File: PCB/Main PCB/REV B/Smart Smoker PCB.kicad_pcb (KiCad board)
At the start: 4 copper layers, 100 x 100 mm, 161 parts, among them J1 393570002, J10 Spare2, J2 Conn_01x03_Female, J3 1051330001, J4 Hopper, J5 393570002, J6 393570002, J7 Screen, J8 393570002, J9 Spare1, Q1 2N7002, Q2 2N7002, Q3 MBT3904DW1, Q4 2N7002, U1 AMS1117-3.3, U10 ALDP105W, U11 TLP2362TPR_E, U12 ALDP105W, U13 STM811SW16F, U2 TS5A23159DGS, U3 ESP32-WROOM-32UE_16MB, U4 MAX31855KASA, U5 TPS2115APWR, U6 TLP2362TPR_E, U7 ALDP105W, U8 CP2102N-A02-GQFN24, U9 TLP2362TPR_E

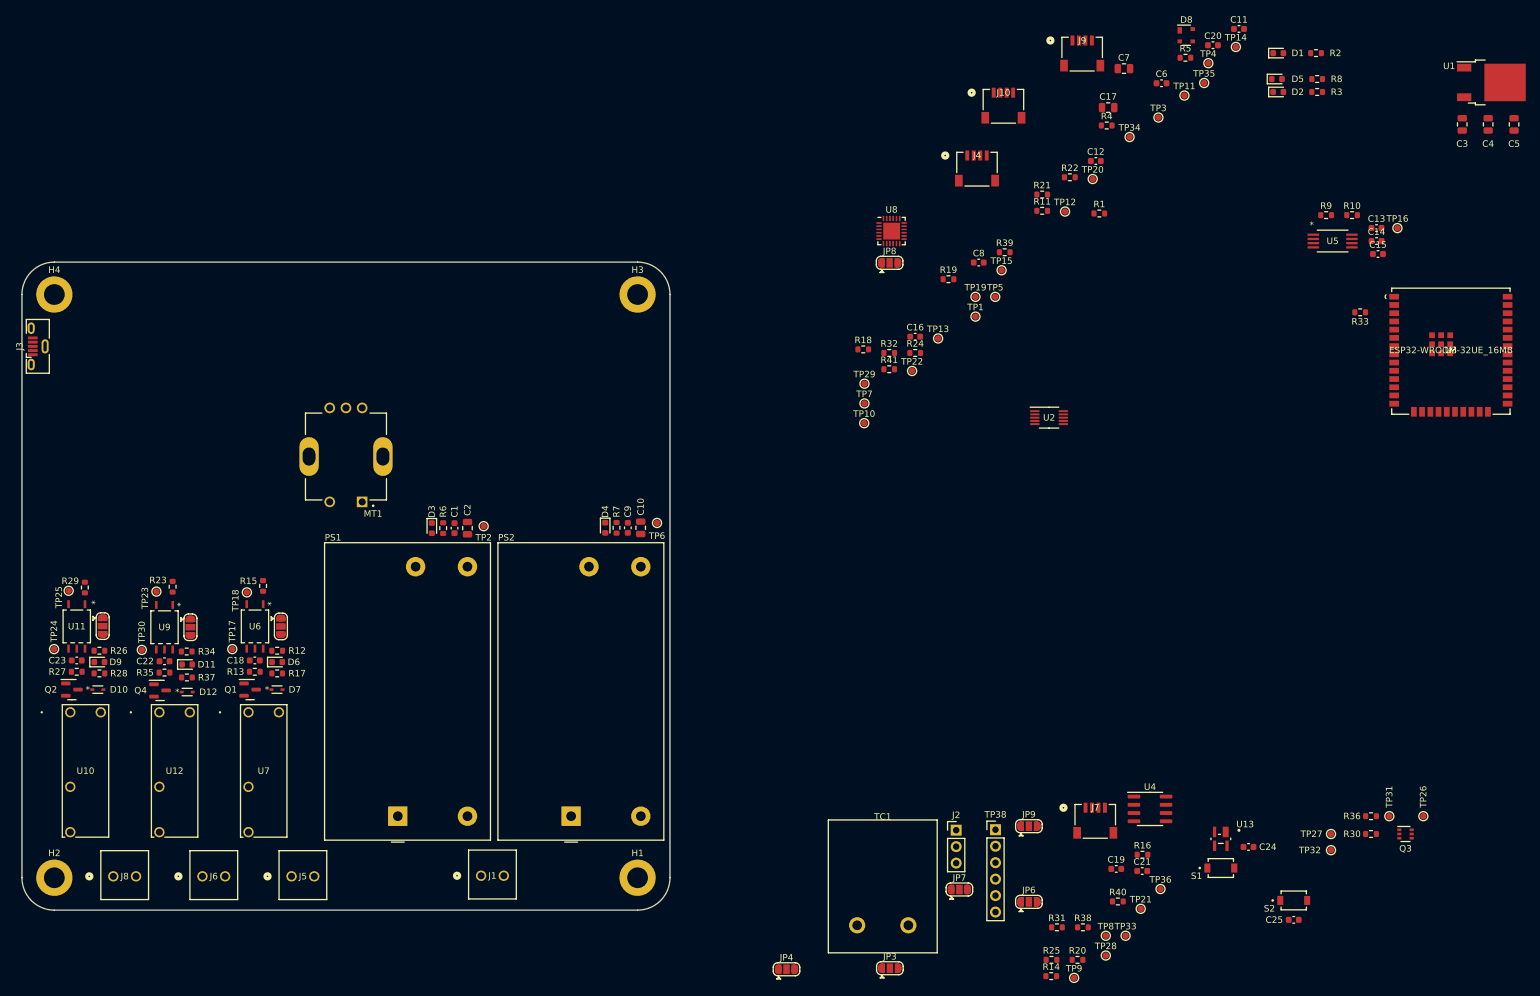
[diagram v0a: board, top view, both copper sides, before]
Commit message: PCB Layout - Work on rotary footprint, change usb to horizontal
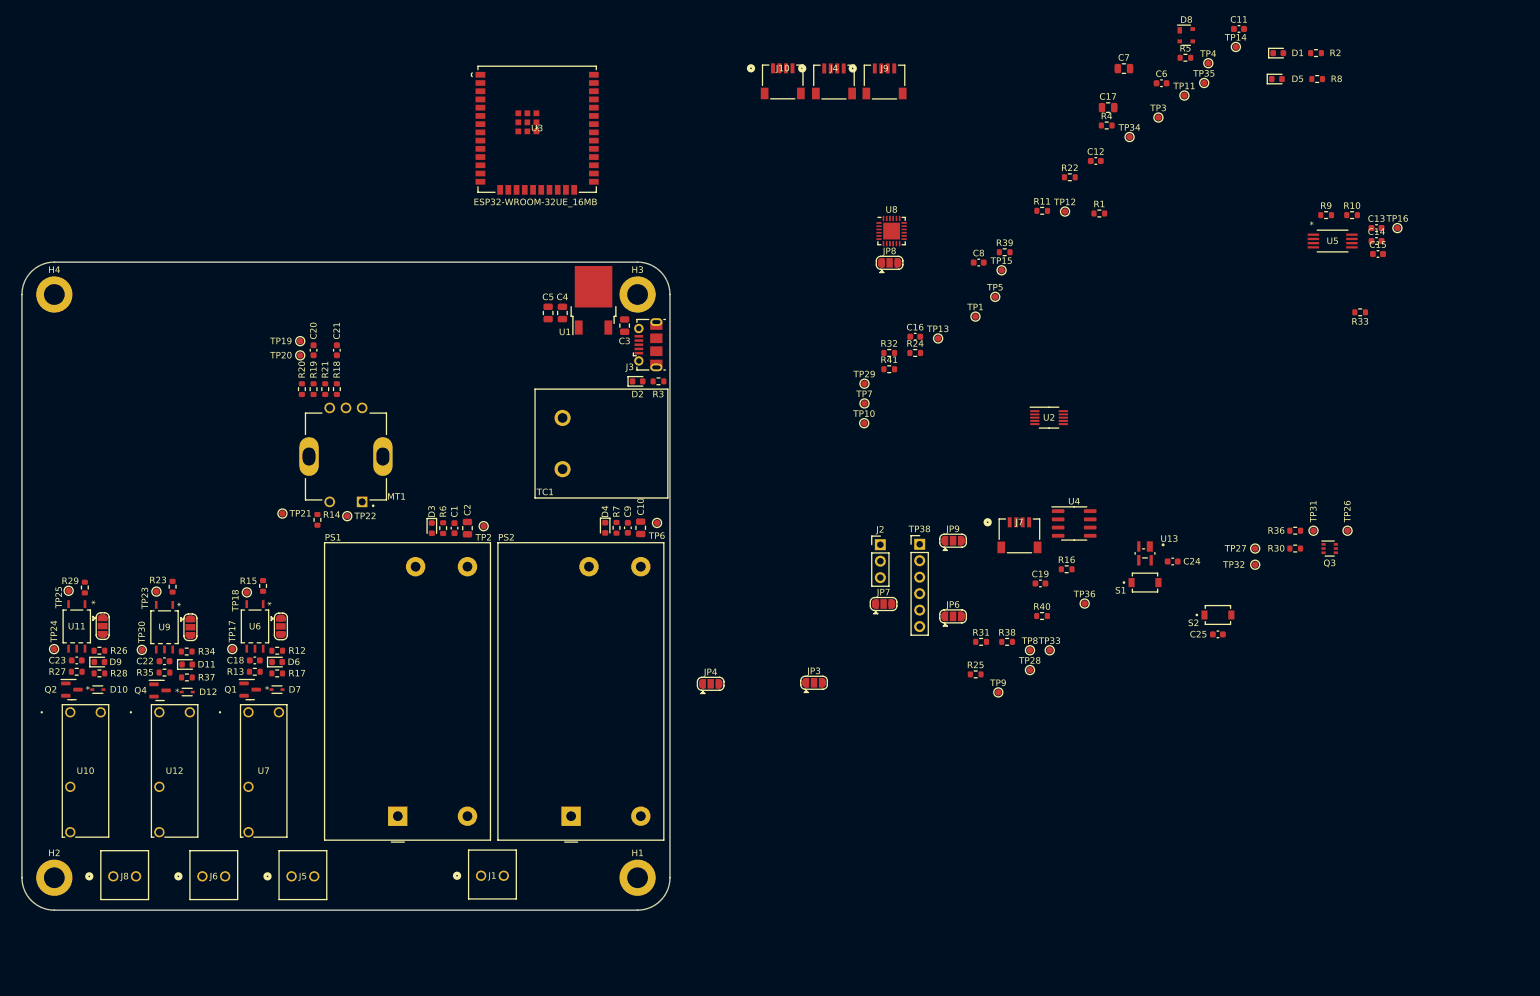
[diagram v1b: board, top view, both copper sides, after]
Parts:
- J3: value 1051330001 -> 1050170001; footprint Connector_USB:USB_Micro-B_Molex-105133-0001 -> Connector_USB:USB_Micro-B_Molex-105017-0001
- moved C5 151.9 mm to (131.2, 57.9)
- moved R20 148.6 mm to (93.2, 69.6), turned to -90 degrees
- moved C21 148.0 mm to (98.6, 63.6), turned to 90 degrees
- moved C20 146.6 mm to (95.0, 63.6), turned to 90 degrees
- moved TP21 145.8 mm to (90.2, 88.8)
- moved C4 145.8 mm to (133.4, 57.9)
- moved U3 145.1 mm to (129.5, 29.5)
- moved U1 142.6 mm to (138.2, 55.9), turned to 90 degrees
- moved R14 133.3 mm to (95.6, 89.8), turned to -90 degrees
- moved C3 132.9 mm to (143.0, 59.8), turned to 90 degrees
- moved TP20 125.3 mm to (92.9, 64.4)
- moved R21 114.6 mm to (96.8, 69.6), turned to -90 degrees
- moved R3 111.0 mm to (148.2, 68.4)
- moved D2 108.5 mm to (145.0, 68.4)
- moved TP19 104.4 mm to (92.9, 62.2)
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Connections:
- TP21 pad 1: /IO33 -> /IO34
